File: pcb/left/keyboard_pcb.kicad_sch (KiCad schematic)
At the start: 105 parts, among them J3 Alt. Battery, J4 Conn_01x01_Socket, K00 KEYSW, K01 KEYSW, K02 KEYSW, K03 KEYSW, K04 KEYSW, K05 KEYSW, K10 KEYSW, K11 KEYSW, K12 KEYSW, K13 KEYSW, K14 KEYSW, K15 KEYSW, K20 KEYSW, K21 KEYSW, K22 KEYSW, K23 KEYSW, K24 KEYSW, K25 KEYSW, K33 KEYSW, K34 KEYSW, K35 KEYSW, U1 Flippable RP2040 ProMicro/nic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

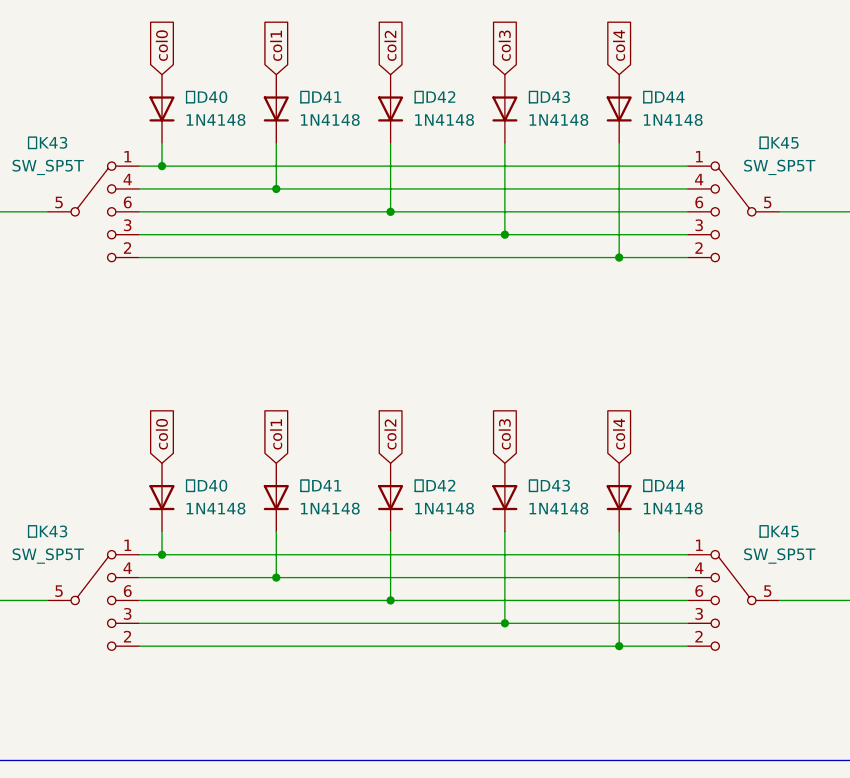
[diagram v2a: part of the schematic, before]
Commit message: Connect left and right nav. switch nets to allow for easier routing
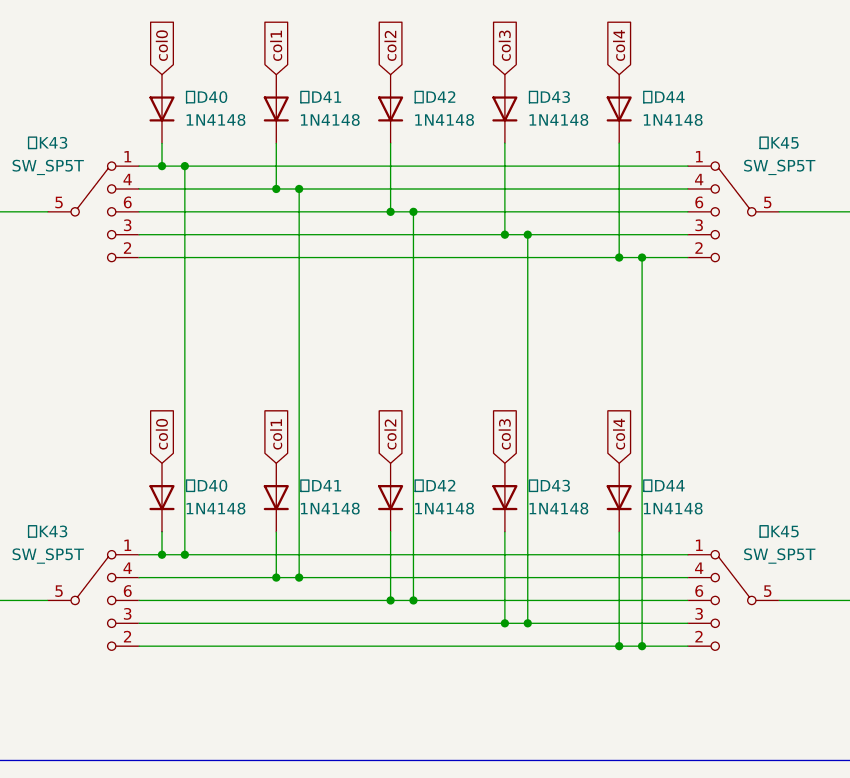
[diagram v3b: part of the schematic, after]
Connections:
- net at 左D42.1 (K), 左K43.6 (D), 左K45.6 (D): now also 右D42.1 (K), 右K43.6 (D), 右K45.6 (D)
- net at 左D43.1 (K), 左K43.3 (C), 左K45.3 (C): now also 右D43.1 (K), 右K43.3 (C), 右K45.3 (C)
- net at 左D40.1 (K), 左K43.1 (A), 左K45.1 (A): now also 右D40.1 (K), 右K43.1 (A), 右K45.1 (A)
- net at 左D44.1 (K), 左K43.2 (Ctr), 左K45.2 (Ctr): now also 右D44.1 (K), 右K43.2 (Ctr), 右K45.2 (Ctr)
- net at 左D41.1 (K), 左K43.4 (B), 左K45.4 (B): now also 右D41.1 (K), 右K43.4 (B), 右K45.4 (B)
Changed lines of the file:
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@@
   (junction (at 259.08 144.78) (diameter 0) (color 0 0 0 0)
   )
+  (junction (at 203.2 259.08) (diameter 0) (color 0 0 0 0)
+  )
   (junction (at 314.96 152.4) (diameter 0) (color 0 0 0 0)
   )
@@
   (junction (at 271.78 127) (diameter 0) (color 0 0 0 0)
   )
+  (junction (at 203.2 215.9) (diameter 0) (color 0 0 0 0)
+  )
   (junction (at 228.6 116.84) (diameter 0) (color 0 0 0 0)
   )
@@
   (junction (at 259.08 127) (diameter 0) (color 0 0 0 0)
   )
+  (junction (at 177.8 210.82) (diameter 0) (color 0 0 0 0)
+  )
   (junction (at 314.96 116.84) (diameter 0) (color 0 0 0 0)
   )
+  (junction (at 177.8 254) (diameter 0) (color 0 0 0 0)
+  )
   (junction (at 271.78 109.22) (diameter 0) (color 0 0 0 0)
   )
   (junction (at 167.64 134.62) (diameter 0) (color 0 0 0 0)
   )
+  (junction (at 215.9 261.62) (diameter 0) (color 0 0 0 0)
+  )
   (junction (at 180.34 127) (diameter 0) (color 0 0 0 0)
   )
@@
   (junction (at 223.52 134.62) (diameter 0) (color 0 0 0 0)
   )
+  (junction (at 190.5 256.54) (diameter 0) (color 0 0 0 0)
+  )
   (junction (at 332.74 109.22) (diameter 0) (color 0 0 0 0)
   )
@@
   (junction (at 35.56 127) (diameter 0) (color 0 0 0 0)
   )
+  (junction (at 215.9 218.44) (diameter 0) (color 0 0 0 0)
+  )
   (junction (at 320.04 162.56) (diameter 0) (color 0 0 0 0)
   )
@@
   (junction (at 271.78 144.78) (diameter 0) (color 0 0 0 0)
   )
+  (junction (at 228.6 220.98) (diameter 0) (color 0 0 0 0)
+  )
   (junction (at 289.56 134.62) (diameter 0) (color 0 0 0 0)
   )
@@
   (junction (at 198.12 109.22) (diameter 0) (color 0 0 0 0)
   )
+  (junction (at 190.5 213.36) (diameter 0) (color 0 0 0 0)
+  )
   (junction (at 213.36 218.44) (diameter 0) (color 0 0 0 0)
   )
@@
   )
   (junction (at 198.12 152.4) (diameter 0) (color 0 0 0 0)
+  )
+  (junction (at 228.6 264.16) (diameter 0) (color 0 0 0 0)
   )
   (junction (at 284.48 170.18) (diameter 0) (color 0 0 0 0)
@@
     (stroke (width 0) (type default))
   )
+  (wire (pts (xy 190.5 213.36) (xy 190.5 256.54))
+    (stroke (width 0) (type default))
+  )
   (wire (pts (xy 314.96 144.78) (xy 320.04 144.78))
     (stroke (width 0) (type default))
   )
-  (wire (pts (xy 175.26 210.82) (xy 233.68 210.82))
+  (wire (pts (xy 175.26 210.82) (xy 177.8 210.82))
     (stroke (width 0) (type default))
   )
@@
     (stroke (width 0) (type default))
   )
-  (wire (pts (xy 213.36 218.44) (xy 233.68 218.44))
+  (wire (pts (xy 213.36 218.44) (xy 215.9 218.44))
     (stroke (width 0) (type default))
   )
@@
     (stroke (width 0) (type default))
   )
-  (wire (pts (xy 200.66 259.08) (xy 233.68 259.08))
+  (wire (pts (xy 200.66 259.08) (xy 203.2 259.08))
     (stroke (width 0) (type default))
   )
@@
     (stroke (width 0) (type default))
   )
+  (wire (pts (xy 177.8 254) (xy 233.68 254))
+    (stroke (width 0) (type default))
+  )
   (wire (pts (xy 223.52 144.78) (xy 228.6 144.78))
     (stroke (width 0) (type default))
@@
     (stroke (width 0) (type default))
   )
-  (wire (pts (xy 213.36 261.62) (xy 233.68 261.62))
+  (wire (pts (xy 190.5 256.54) (xy 233.68 256.54))
+    (stroke (width 0) (type default))
+  )
+  (wire (pts (xy 228.6 264.16) (xy 233.68 264.16))
+    (stroke (width 0) (type default))
+  )
+  (wire (pts (xy 213.36 261.62) (xy 215.9 261.62))
     (stroke (width 0) (type default))
   )
@@
     (stroke (width 0) (type default))
   )
+  (wire (pts (xy 177.8 210.82) (xy 233.68 210.82))
+    (stroke (width 0) (type default))
+  )
   (wire (pts (xy 152.4 170.18) (xy 254 170.18))
     (stroke (width 0) (type default))
@@
     (stroke (width 0) (type default))
   )
+  (wire (pts (xy 215.9 218.44) (xy 215.9 261.62))
+    (stroke (width 0) (type default))
+  )
   (wire (pts (xy 106.68 210.82) (xy 106.68 213.36))
     (stroke (width 0) (type default))
@@
     (stroke (width 0) (type default))
   )
+  (wire (pts (xy 190.5 213.36) (xy 233.68 213.36))
+    (stroke (width 0) (type default))
+  )
   (wire (pts (xy 254 144.78) (xy 259.08 144.78))
     (stroke (width 0) (type default))
@@
     (stroke (width 0) (type default))
   )
+  (wire (pts (xy 215.9 261.62) (xy 233.68 261.62))
+    (stroke (width 0) (type default))
+  )
   (wire (pts (xy 55.88 154.94) (xy 53.34 154.94))
     (stroke (width 0) (type default))
@@
     (stroke (width 0) (type default))
   )
-  (wire (pts (xy 226.06 220.98) (xy 233.68 220.98))
+  (wire (pts (xy 226.06 220.98) (xy 228.6 220.98))
     (stroke (width 0) (type default))
   )
@@
     (stroke (width 0) (type default))
   )
-  (wire (pts (xy 200.66 215.9) (xy 233.68 215.9))
+  (wire (pts (xy 200.66 215.9) (xy 203.2 215.9))
     (stroke (width 0) (type default))
   )
@@
     (stroke (width 0) (type default))
   )
+  (wire (pts (xy 215.9 218.44) (xy 233.68 218.44))
+    (stroke (width 0) (type default))
+  )
   (wire (pts (xy 314.96 116.84) (xy 320.04 116.84))
     (stroke (width 0) (type default))
@@
     (stroke (width 0) (type default))
   )
+  (wire (pts (xy 177.8 210.82) (xy 177.8 254))
+    (stroke (width 0) (type default))
+  )
   (wire (pts (xy 284.48 162.56) (xy 289.56 162.56))
     (stroke (width 0) (type default))
@@
     (stroke (width 0) (type default))
   )
-  (wire (pts (xy 187.96 213.36) (xy 233.68 213.36))
+  (wire (pts (xy 187.96 213.36) (xy 190.5 213.36))
     (stroke (width 0) (type default))
   )
@@
     (stroke (width 0) (type default))
   )
+  (wire (pts (xy 203.2 259.08) (xy 233.68 259.08))
+    (stroke (width 0) (type default))
+  )
   (wire (pts (xy 193.04 134.62) (xy 198.12 134.62))
     (stroke (width 0) (type default))
@@
     (stroke (width 0) (type default))
   )
-  (wire (pts (xy 226.06 264.16) (xy 233.68 264.16))
+  (wire (pts (xy 226.06 264.16) (xy 228.6 264.16))
     (stroke (width 0) (type default))
   )
@@
     (stroke (width 0) (type default))
   )
+  (wire (pts (xy 228.6 220.98) (xy 228.6 264.16))
+    (stroke (width 0) (type default))
+  )
   (wire (pts (xy 88.9 40.64) (xy 86.36 40.64))
     (stroke (width 0) (type default))
@@
     (stroke (width 0) (type default))
   )
-  (wire (pts (xy 187.96 256.54) (xy 233.68 256.54))
+  (wire (pts (xy 187.96 256.54) (xy 190.5 256.54))
     (stroke (width 0) (type default))
   )
@@
     (stroke (width 0) (type default))
   )
-  (wire (pts (xy 175.26 254) (xy 233.68 254))
+  (wire (pts (xy 175.26 254) (xy 177.8 254))
     (stroke (width 0) (type default))
   )
@@
     (stroke (width 0) (type default))
   )
+  (wire (pts (xy 228.6 220.98) (xy 233.68 220.98))
+    (stroke (width 0) (type default))
+  )
   (wire (pts (xy 172.72 213.36) (xy 187.96 213.36))
     (stroke (width 0) (type default))
@@
     (stroke (width 0) (type default))
   )
+  (wire (pts (xy 203.2 215.9) (xy 203.2 259.08))
+    (stroke (width 0) (type default))
+  )
   (wire (pts (xy 55.88 154.94) (xy 55.88 157.48))
     (stroke (width 0) (type default))
@@
     (stroke (width 0) (type default))
   )
+  (wire (pts (xy 203.2 215.9) (xy 233.68 215.9))
+    (stroke (width 0) (type default))
+  )

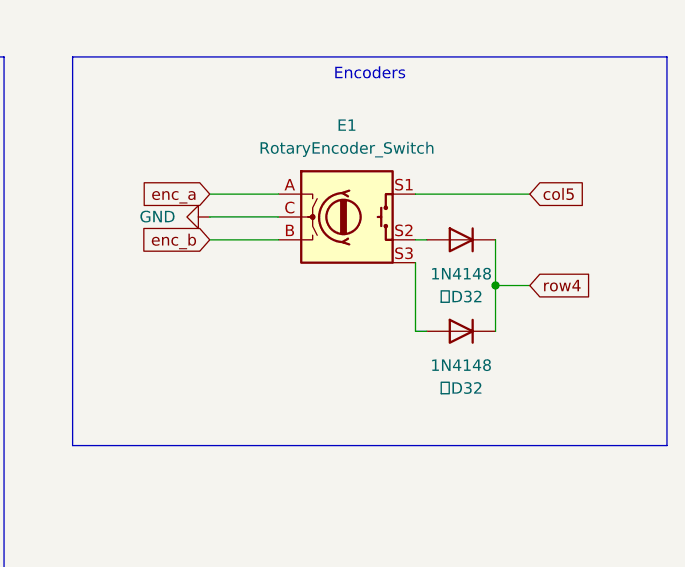
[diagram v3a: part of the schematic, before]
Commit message: Move encoder diode outside encoder footprint
Want to add a standoff under the encoder, so can’t have a component there!
Updated schematic between encoder and diode to simplify routing.
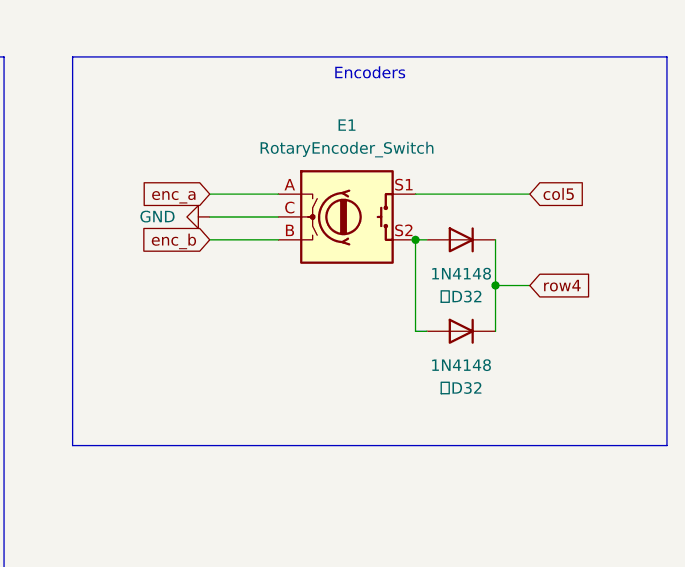
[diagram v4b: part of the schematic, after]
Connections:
- net at E1.S2, 左D32.2 (A): now also 右D32.2 (A)
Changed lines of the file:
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@@
   (junction (at 302.26 144.78) (diameter 0) (color 0 0 0 0)
   )
+  (junction (at 312.42 205.74) (diameter 0) (color 0 0 0 0)
+  )
   (junction (at 193.04 116.84) (diameter 0) (color 0 0 0 0)
   )
@@
     (stroke (width 0) (type default))
   )
-  (wire (pts (xy 312.42 208.28) (xy 312.42 215.9))
+  (wire (pts (xy 312.42 205.74) (xy 312.42 215.9))
     (stroke (width 0) (type default))
   )
@@
     (pin "A")
     (pin "C")
-    (pin "S3")
     (instances
       (project "keyboard_pcb"

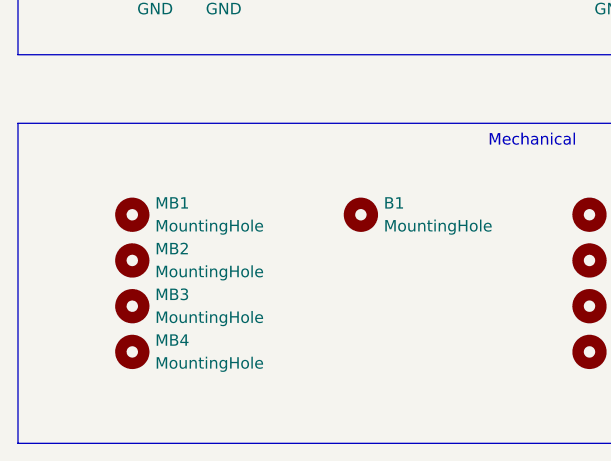
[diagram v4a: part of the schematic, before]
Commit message: Remove mouse bites
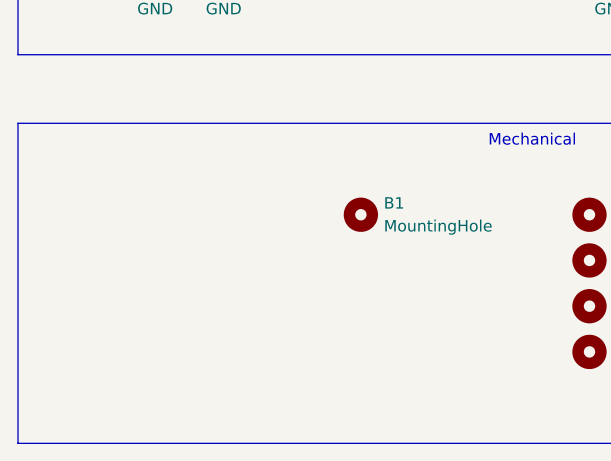
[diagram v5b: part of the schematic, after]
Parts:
- removed MB1, MB2, MB3, MB4: MountingHole, beekeeb_lib:mousebites, symbol Mechanical:MountingHole
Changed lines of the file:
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@@
-    )
-  )
-  (symbol (lib_id "Mechanical:MountingHole") (at 30.48 261.62 0) (unit 1)
-    (in_bom yes) (on_board yes) (dnp no) (fields_autoplaced)
-    (property "Reference" "MB3" (at 33.02 260.3499 0)
-      (effects (font (size 1.27 1.27)) (justify left))
-    )
-    (property "Value" "MountingHole" (at 33.02 262.8899 0)
-      (effects (font (size 1.27 1.27)) (justify left))
-    )
-    (property "Footprint" "beekeeb_lib:mousebites" (at 30.48 261.62 0)
-      (effects (font (size 1.27 1.27)) hide)
-    )
-    (property "Datasheet" "~" (at 30.48 261.62 0)
-      (effects (font (size 1.27 1.27)) hide)
-    )
-    (instances
-      (project "keyboard_pcb"
-        (path "/9538e4ed-27e6-4c37-b989-9859dc0d49e8"
-          (reference "MB3") (unit 1)
-        )
-      )
     )
   )
@@
         (path "/9538e4ed-27e6-4c37-b989-9859dc0d49e8"
           (reference "左D42") (unit 1)
-        )
-      )
-    )
-  )
-  (symbol (lib_id "Mechanical:MountingHole") (at 30.48 256.54 0) (unit 1)
-    (in_bom yes) (on_board yes) (dnp no) (fields_autoplaced)
-    (property "Reference" "MB2" (at 33.02 255.2699 0)
-      (effects (font (size 1.27 1.27)) (justify left))
-    )
-    (property "Value" "MountingHole" (at 33.02 257.8099 0)
-      (effects (font (size 1.27 1.27)) (justify left))
-    )
-    (property "Footprint" "beekeeb_lib:mousebites" (at 30.48 256.54 0)
-      (effects (font (size 1.27 1.27)) hide)
-    )
-    (property "Datasheet" "~" (at 30.48 256.54 0)
-      (effects (font (size 1.27 1.27)) hide)
-    )
-    (instances
-      (project "keyboard_pcb"
-        (path "/9538e4ed-27e6-4c37-b989-9859dc0d49e8"
-          (reference "MB2") (unit 1)
         )
       )
@@
         (path "/9538e4ed-27e6-4c37-b989-9859dc0d49e8"
           (reference "右K43") (unit 1)
-        )
-      )
-    )
-  )
-  (symbol (lib_id "Mechanical:MountingHole") (at 30.48 251.46 0) (unit 1)
-    (in_bom yes) (on_board yes) (dnp no) (fields_autoplaced)
-    (property "Reference" "MB1" (at 33.02 250.1899 0)
-      (effects (font (size 1.27 1.27)) (justify left))
-    )
-    (property "Value" "MountingHole" (at 33.02 252.7299 0)
-      (effects (font (size 1.27 1.27)) (justify left))
-    )
-    (property "Footprint" "beekeeb_lib:mousebites" (at 30.48 251.46 0)
-      (effects (font (size 1.27 1.27)) hide)
-    )
-    (property "Datasheet" "~" (at 30.48 251.46 0)
-      (effects (font (size 1.27 1.27)) hide)
-    )
-    (instances
-      (project "keyboard_pcb"
-        (path "/9538e4ed-27e6-4c37-b989-9859dc0d49e8"
-          (reference "MB1") (unit 1)
         )
       )
@@
         )
       )
-    )
-  )
-  (symbol (lib_id "Mechanical:MountingHole") (at 30.48 266.7 0) (unit 1)
-    (in_bom yes) (on_board yes) (dnp no) (fields_autoplaced)
-    (property "Reference" "MB4" (at 33.02 265.4299 0)
-      (effects (font (size 1.27 1.27)) (justify left))
-    )
-    (property "Value" "MountingHole" (at 33.02 267.9699 0)
-      (effects (font (size 1.27 1.27)) (justify left))
-    )
-    (property "Footprint" "beekeeb_lib:mousebites" (at 30.48 266.7 0)
-      (effects (font (size 1.27 1.27)) hide)
-    )
-    (property "Datasheet" "~" (at 30.48 266.7 0)
-      (effects (font (size 1.27 1.27)) hide)
-    )
-    (instances
-      (project "keyboard_pcb"
-        (path "/9538e4ed-27e6-4c37-b989-9859dc0d49e8"
-          (reference "MB4") (unit 1)
-        )
-      )

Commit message: Fix silkscreen warnings reported by DRC
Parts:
- 右D40, 右D41, 右D42, 右D43, 右D44, 左D40, 左D41, 左D42, 左D43, 左D44: footprint ♥Project_Library:D_SOD-123 -> ♥Project_Library:D_SOD-123_Centre_Label
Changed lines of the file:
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@@
       (effects (font (size 1.27 1.27)) (justify right))
     )
-    (property "Footprint" "♥Project_Library:D_SOD-123" (at 200.66 204.47 0)
+    (property "Footprint" "♥Project_Library:D_SOD-123_Centre_Label" (at 200.66 204.47 0)
       (effects (font (size 1.27 1.27)) hide)
     )
@@
       (effects (font (size 1.27 1.27)) (justify right))
     )
-    (property "Footprint" "♥Project_Library:D_SOD-123" (at 200.66 247.65 0)
+    (property "Footprint" "♥Project_Library:D_SOD-123_Centre_Label" (at 200.66 247.65 0)
       (effects (font (size 1.27 1.27)) hide)
     )
@@
       (effects (font (size 1.27 1.27)) (justify right))
     )
-    (property "Footprint" "♥Project_Library:D_SOD-123" (at 213.36 204.47 0)
+    (property "Footprint" "♥Project_Library:D_SOD-123_Centre_Label" (at 213.36 204.47 0)
       (effects (font (size 1.27 1.27)) hide)
     )
@@
       (effects (font (size 1.27 1.27)) (justify right))
     )
-    (property "Footprint" "♥Project_Library:D_SOD-123" (at 175.26 204.47 0)
+    (property "Footprint" "♥Project_Library:D_SOD-123_Centre_Label" (at 175.26 204.47 0)
       (effects (font (size 1.27 1.27)) hide)
     )
@@
       (effects (font (size 1.27 1.27)) (justify right))
     )
-    (property "Footprint" "♥Project_Library:D_SOD-123" (at 226.06 247.65 0)
+    (property "Footprint" "♥Project_Library:D_SOD-123_Centre_Label" (at 226.06 247.65 0)
       (effects (font (size 1.27 1.27)) hide)
     )
@@
       (effects (font (size 1.27 1.27)) (justify right))
     )
-    (property "Footprint" "♥Project_Library:D_SOD-123" (at 213.36 247.65 0)
+    (property "Footprint" "♥Project_Library:D_SOD-123_Centre_Label" (at 213.36 247.65 0)
       (effects (font (size 1.27 1.27)) hide)
     )
@@
       (effects (font (size 1.27 1.27)) (justify right))
     )
-    (property "Footprint" "♥Project_Library:D_SOD-123" (at 226.06 204.47 0)
+    (property "Footprint" "♥Project_Library:D_SOD-123_Centre_Label" (at 226.06 204.47 0)
       (effects (font (size 1.27 1.27)) hide)
     )
@@
       (effects (font (size 1.27 1.27)) (justify right))
     )
-    (property "Footprint" "♥Project_Library:D_SOD-123" (at 175.26 247.65 0)
+    (property "Footprint" "♥Project_Library:D_SOD-123_Centre_Label" (at 175.26 247.65 0)
       (effects (font (size 1.27 1.27)) hide)
     )
@@
       (effects (font (size 1.27 1.27)) (justify right))
     )
-    (property "Footprint" "♥Project_Library:D_SOD-123" (at 187.96 204.47 0)
+    (property "Footprint" "♥Project_Library:D_SOD-123_Centre_Label" (at 187.96 204.47 0)
       (effects (font (size 1.27 1.27)) hide)
     )
@@
       (effects (font (size 1.27 1.27)) (justify right))
     )
-    (property "Footprint" "♥Project_Library:D_SOD-123" (at 187.96 247.65 0)
-      (effects (font (size 1.27 1.27)) hide)
-    )
+    (property "Footprint" "♥Project_Library:D_SOD-123_Centre_Label" (at 187.96 247.65 0)
+      (effects (font (size 1.27 1.27)) hide)
+    )

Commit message: Reduce size of MCU keep-out, fit silkscreen issues
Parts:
- J4: footprint beekeeb_lib:SinglePad -> Connector_Wire:SolderWire-0.5sqmm_1x01_D0.9mm_OD2.1mm
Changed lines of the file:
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@@
       (effects (font (size 1.27 1.27)) (justify left) hide)
     )
-    (property "Footprint" "beekeeb_lib:SinglePad" (at 63.5 124.46 0)
+    (property "Footprint" "Connector_Wire:SolderWire-0.5sqmm_1x01_D0.9mm_OD2.1mm" (at 63.5 124.46 0)
       (effects (font (size 1.27 1.27)) hide)
     )
